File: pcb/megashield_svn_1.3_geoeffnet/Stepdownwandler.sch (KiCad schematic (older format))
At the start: 18 parts, among them U1 DC 10V, U6 DC 3,3V, U7 DC 5V

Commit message: Platine V1.3
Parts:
- removed R24, R25, R26: 0, ACS712:Resistor_Horizontal_RM15mm, symbol R
- removed ZD1: ZD-5W 3,3V Optional, ACS712:Diode_ligend_RM10, symbol DIODE
- removed ZD2: ZD-5W 5,1 Optional, ACS712:Diode_ligend_RM10, symbol DIODE
- removed ZD3: ZD-5W 12V Optional, ACS712:Diode_ligend_RM10, symbol DIODE
- added DBY13, DBY14, DBY15, DBY16, DBY17, DBY18: BY 500/1000, ACS712:Diode_liegend_BY500_1000_RM15, symbol DIODE
- added DKE5, DKE6, DKE7: 15KE33CA, ACS712:Diode_15KE33CA, symbol 15KEXXC
- added PRFA6, PRFA7: PFRA 040, ACS712:PRFA_500_stehend, symbol F_10A
- added PRFA8: PFRA 040, symbol F_10A
- PRFA3, PRFA4, PRFA5: value PFRA 185 -> PFRA 040; Bestelllink http://www.reichelt.de/index.html?ACTION=3;ARTICLE=35184;SE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 -> https://www.reichelt.de/PFRA-040/3/index.html?&ACTION=3&LA=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; Bestellnummer R: PFRA 185 -> R: PFRA 040
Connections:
- net GND: now also DBY14.1 (A), DBY17.1 (A), DBY18.1 (A), DKE5.2, DKE6.2, DKE7.2
- net Stepdownwandler_24V_In: now also PRFA6.2, PRFA7.2, PRFA8.2; no longer U1.3 (VIN), U6.3 (VIN), U7.3 (VIN)
- net at PRFA3.2, U7.2 (Vout): now also DBY13.1 (A), DBY14.2 (K)
- net at PRFA5.2, U6.2 (Vout): now also DBY16.1 (A), DBY18.2 (K)
- net at PRFA4.2, U1.2 (Vout): now also DBY15.1 (A), DBY17.2 (K)
- new net: DBY13.2 (K), DKE5.1, PRFA6.1, U7.3 (VIN)
- new net: DBY16.2 (K), DKE7.1, PRFA8.1, U6.3 (VIN)
- new net: DBY15.2 (K), DKE6.1, PRFA7.1, U1.3 (VIN)
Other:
- note added: "Jürgen von 6.6.2015 \n3v 400ma eingang ausgang \n5v max 400ma eingang ausgang \n10v max 400ma eingang ausgang\n\nden 100µF ELKO kannst du durch einen 330nF Kerko ersetzen\ndie ELKOS setzen wir z.T an einer anderen Stelle im Board ein\nwo es mehr sinn macht das gehen wir nochmal an"
- note removed: "pfra Sicherung müssen von dem Wert her noch angepasst werden"
- moved on the sheet: C2, C7, C8, PRFA3, PRFA4, U1, U6, U7

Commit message: Platine V1.3
RTC Uhr und INA169 Uhr hinzugefügt
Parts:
- PRFA8: footprint (none) -> ACS712:PRFA_500_stehend
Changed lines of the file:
@@
 LIBS:conn
 LIBS:uln-udn
+LIBS:ina169_ic
+LIBS:DS1307_Dil8
+LIBS:device
+LIBS:supply
 EELAYER 25 0
 EELAYER END
 $Descr A4 11693 8268
 encoding utf-8
-Sheet 19 25
+Sheet 19 26
 Title "Ardumower Shield - Stepdownwandler"
 Date ""
@@
 F 0 "PRFA8" H 3675 3625 40  0000 C CNN
 F 1 "PFRA 040" H 3755 3465 40  0000 C CNN
-F 2 "" H 3855 3545 60  0001 C CNN
+F 2 "ACS712:PRFA_500_stehend" H 3855 3545 60  0001 C CNN
 F 3 "" H 3855 3545 60  0000 C CNN
 F 4 "R: PFRA 040" H 3855 3545 60  0001 C CNN "Bestellnummer"

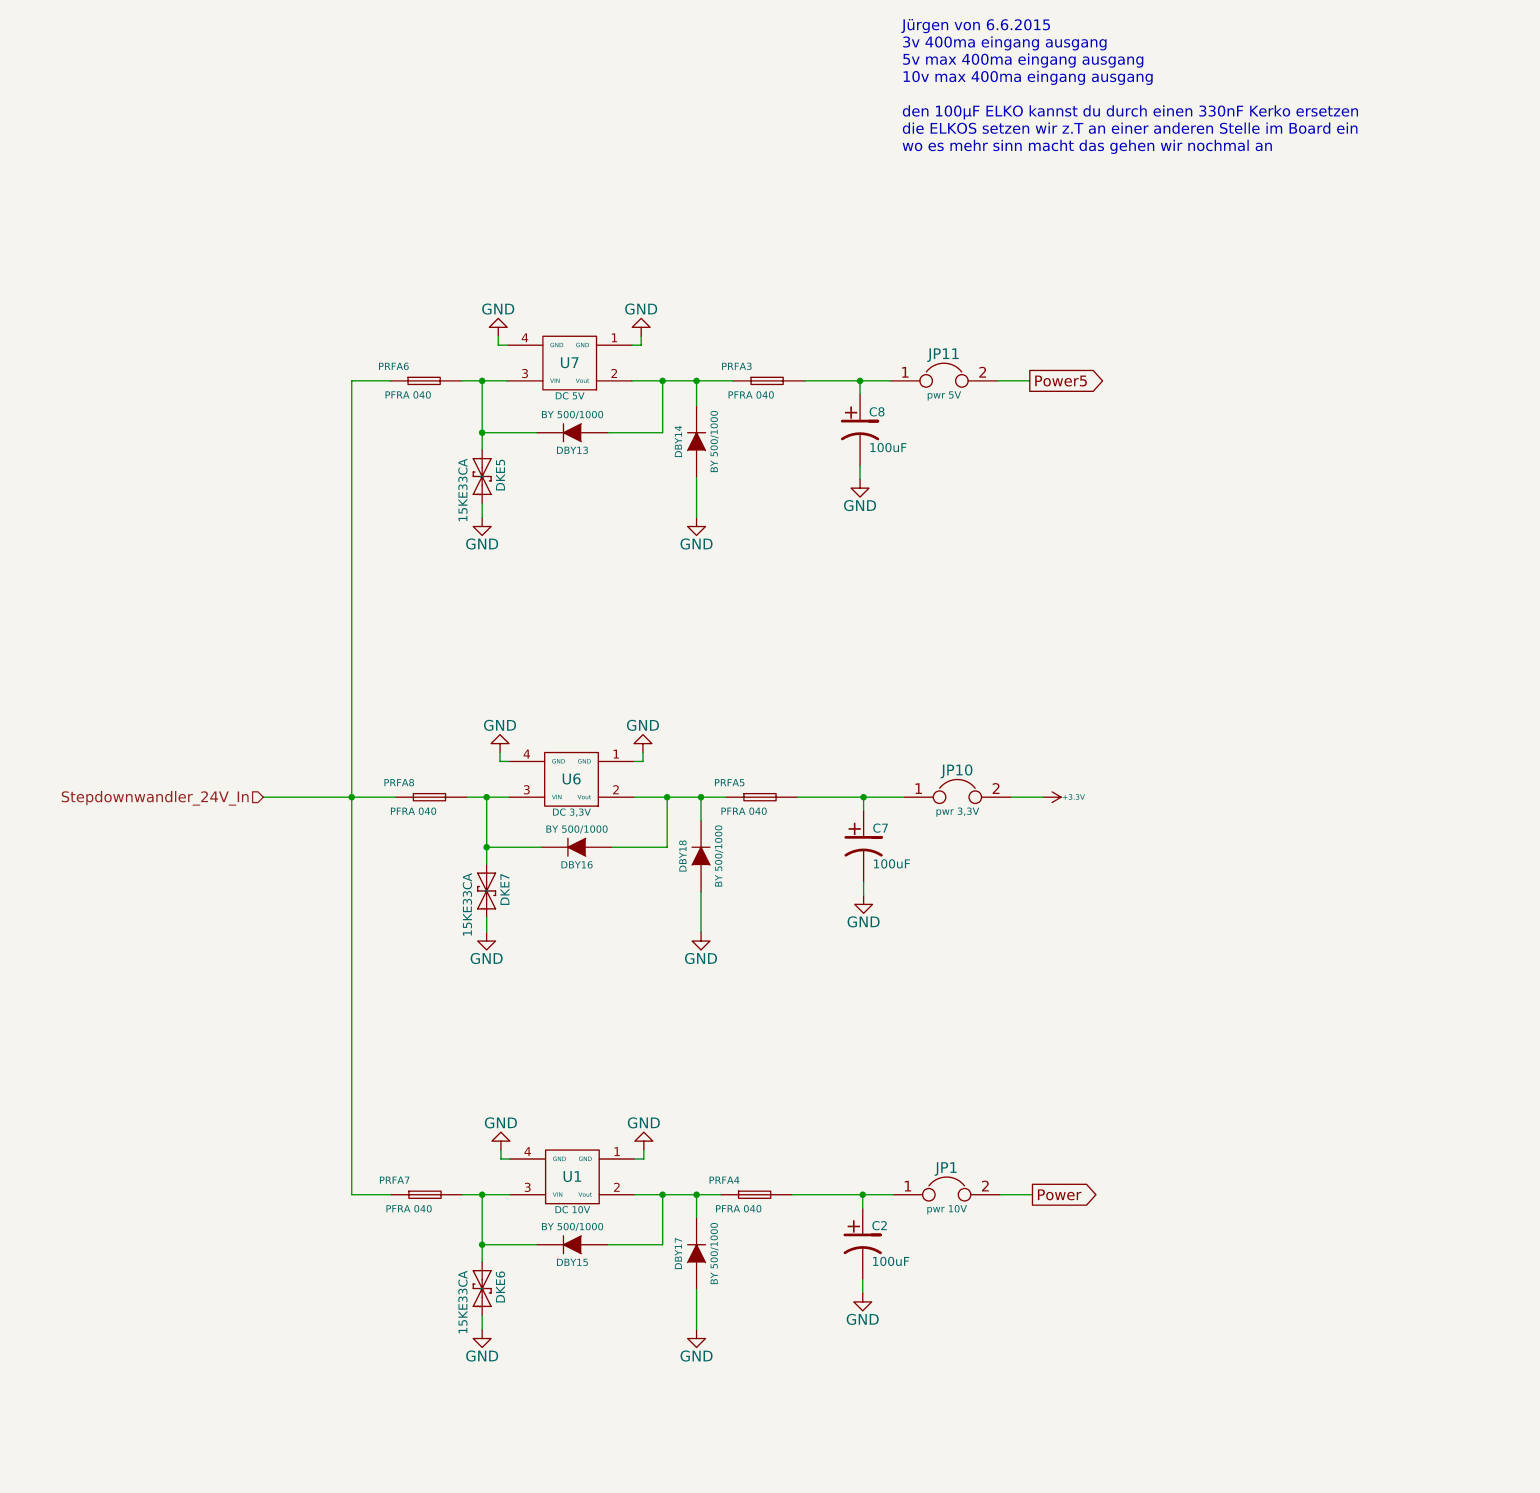
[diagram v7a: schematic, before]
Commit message: Platine V1.3
Arduino Mega auf SMD umgeändert
Spannungsversorgung 5V +3V neu hinzugefügt und DC Wandler entfernt
Programmieranschlüsse hinzugefügt
Anschluss Led - Leiste erweitert
usw........
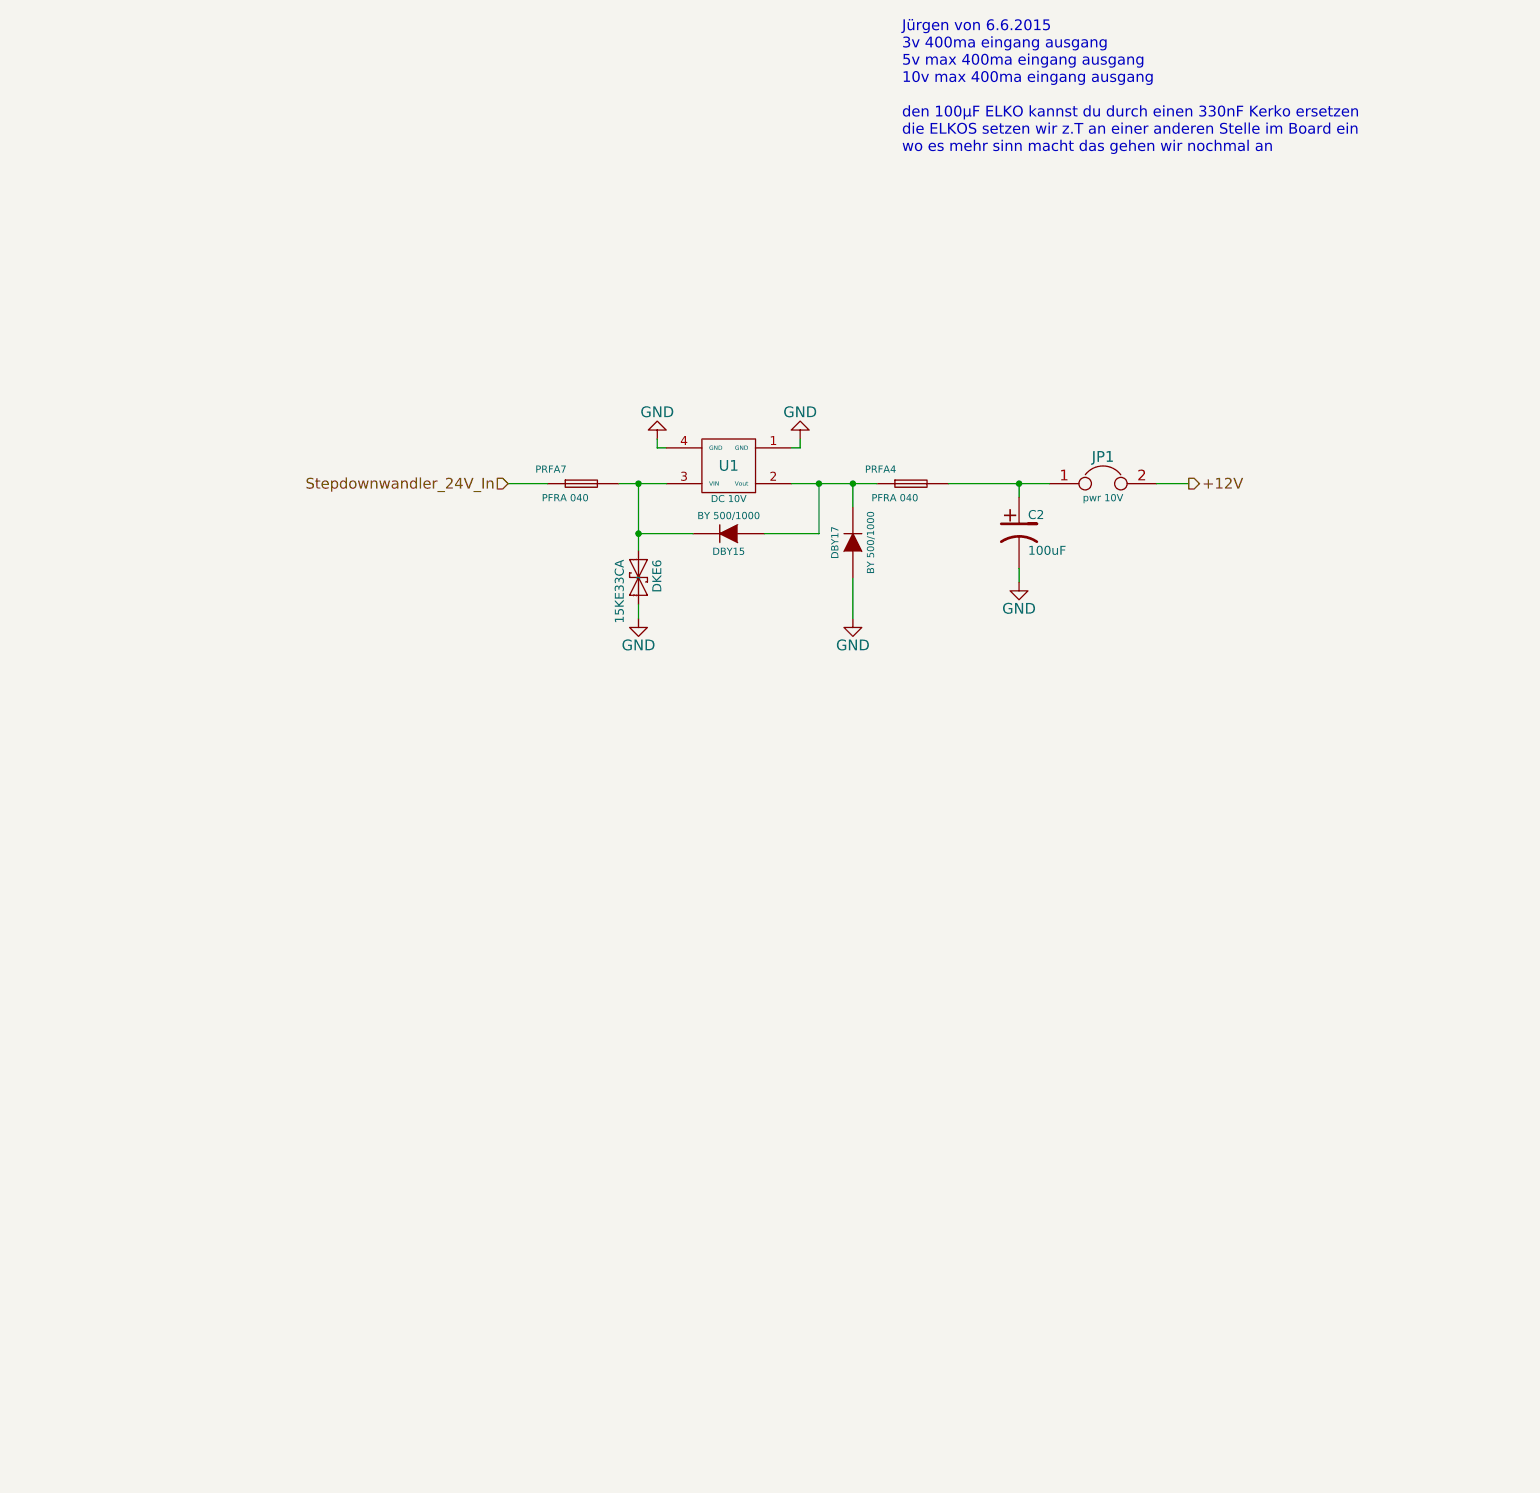
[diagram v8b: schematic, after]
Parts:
- removed C7, C8: 100uF, ACS712:Elko_vert_11.2x6.3mm_RM2.5_RM5.0, symbol CP1
- removed DBY13, DBY14, DBY16, DBY18: BY 500/1000, ACS712:Diode_liegend_BY500_1000_RM15, symbol DIODE
- removed DKE5, DKE7: 15KE33CA, ACS712:Diode_15KE33CA, symbol 15KEXXC
- removed JP10: pwr 3,3V, ACS712:Pin_Header_Straight_1x02, symbol JUMPER
- removed JP11: pwr 5V, ACS712:Pin_Header_Straight_1x02, symbol JUMPER
- removed PRFA3, PRFA5, PRFA6, PRFA8: PFRA 040, ACS712:PRFA_500_stehend, symbol F_10A
- removed U6: DC 3,3V, ACS712:DC_DC_DSN2596_mit_Bohrloch_doppelte_Lochreihe, symbol DC-DC_Stepdown
- removed U7: DC 5V, ACS712:DC_DC_DSN2596_mit_Bohrloch_doppelte_Lochreihe, symbol DC-DC_Stepdown
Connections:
- net Power renamed +12V
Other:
- moved on the sheet: C2, DBY15, DBY17, DKE6, JP1, PRFA4, PRFA7, U1
